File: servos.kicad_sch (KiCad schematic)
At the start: 28 parts, among them J10 Conn_01x03_Male, J5 Conn_01x03_Male, J6 Conn_01x03_Male, J7 Conn_01x03_Male, J8 Conn_01x03_Male, J9 Conn_01x03_Male, U2 MOCD20, U3 MOCD20, U4 MOCD20, U5 MOCD20

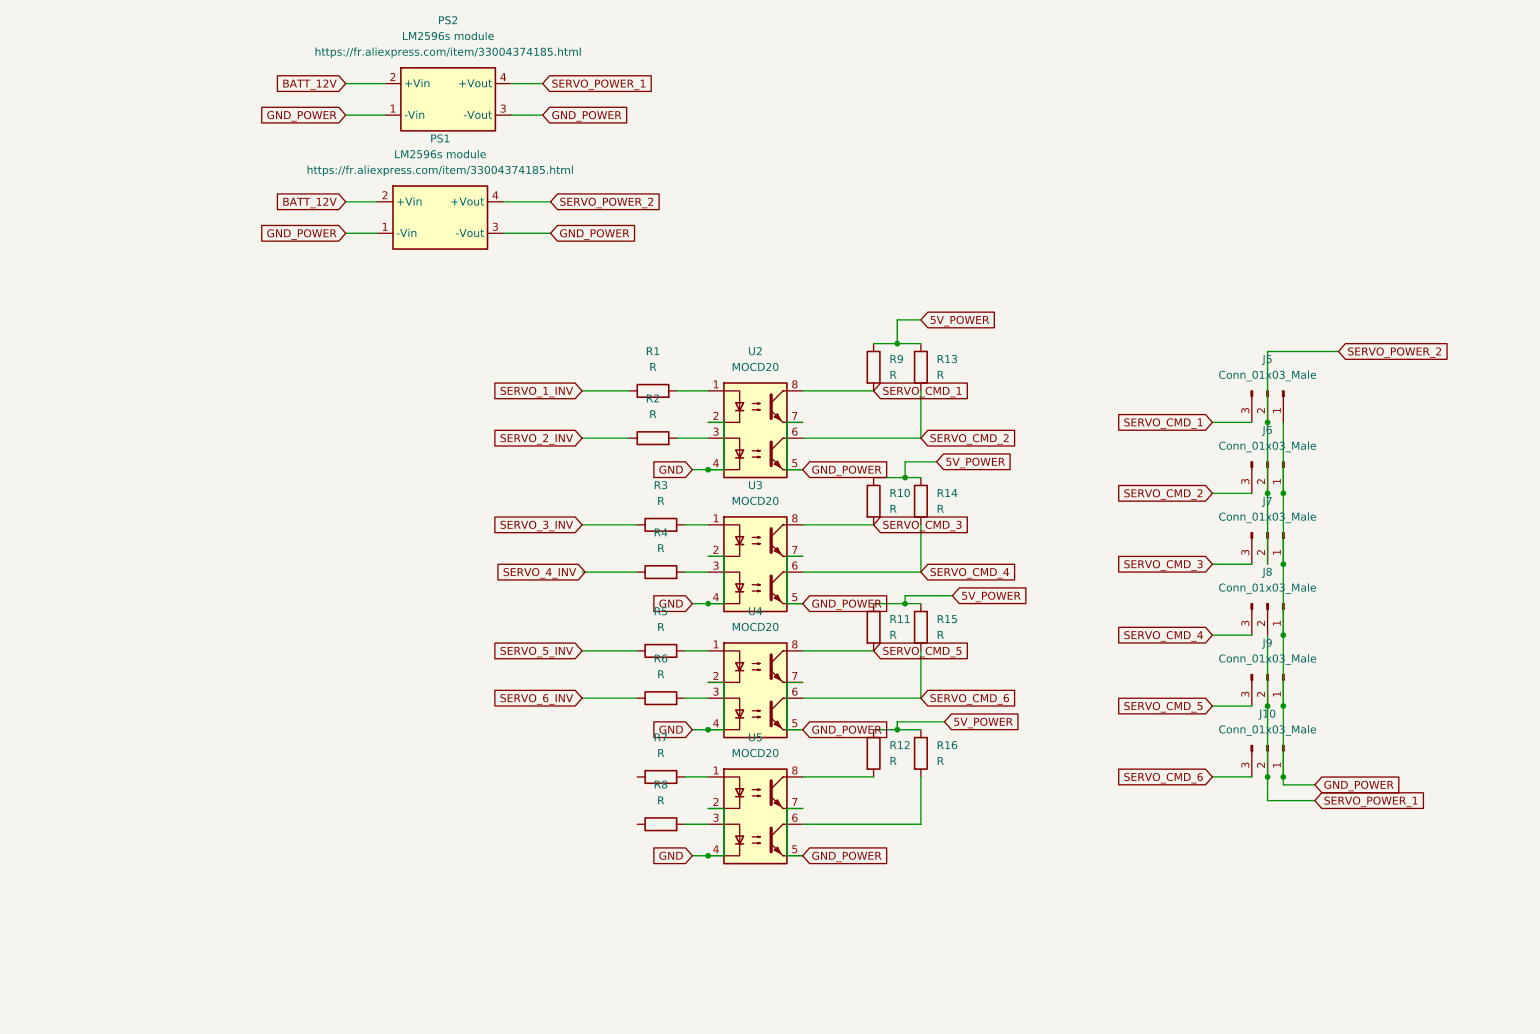
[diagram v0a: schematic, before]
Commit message: version without mega I2C pins
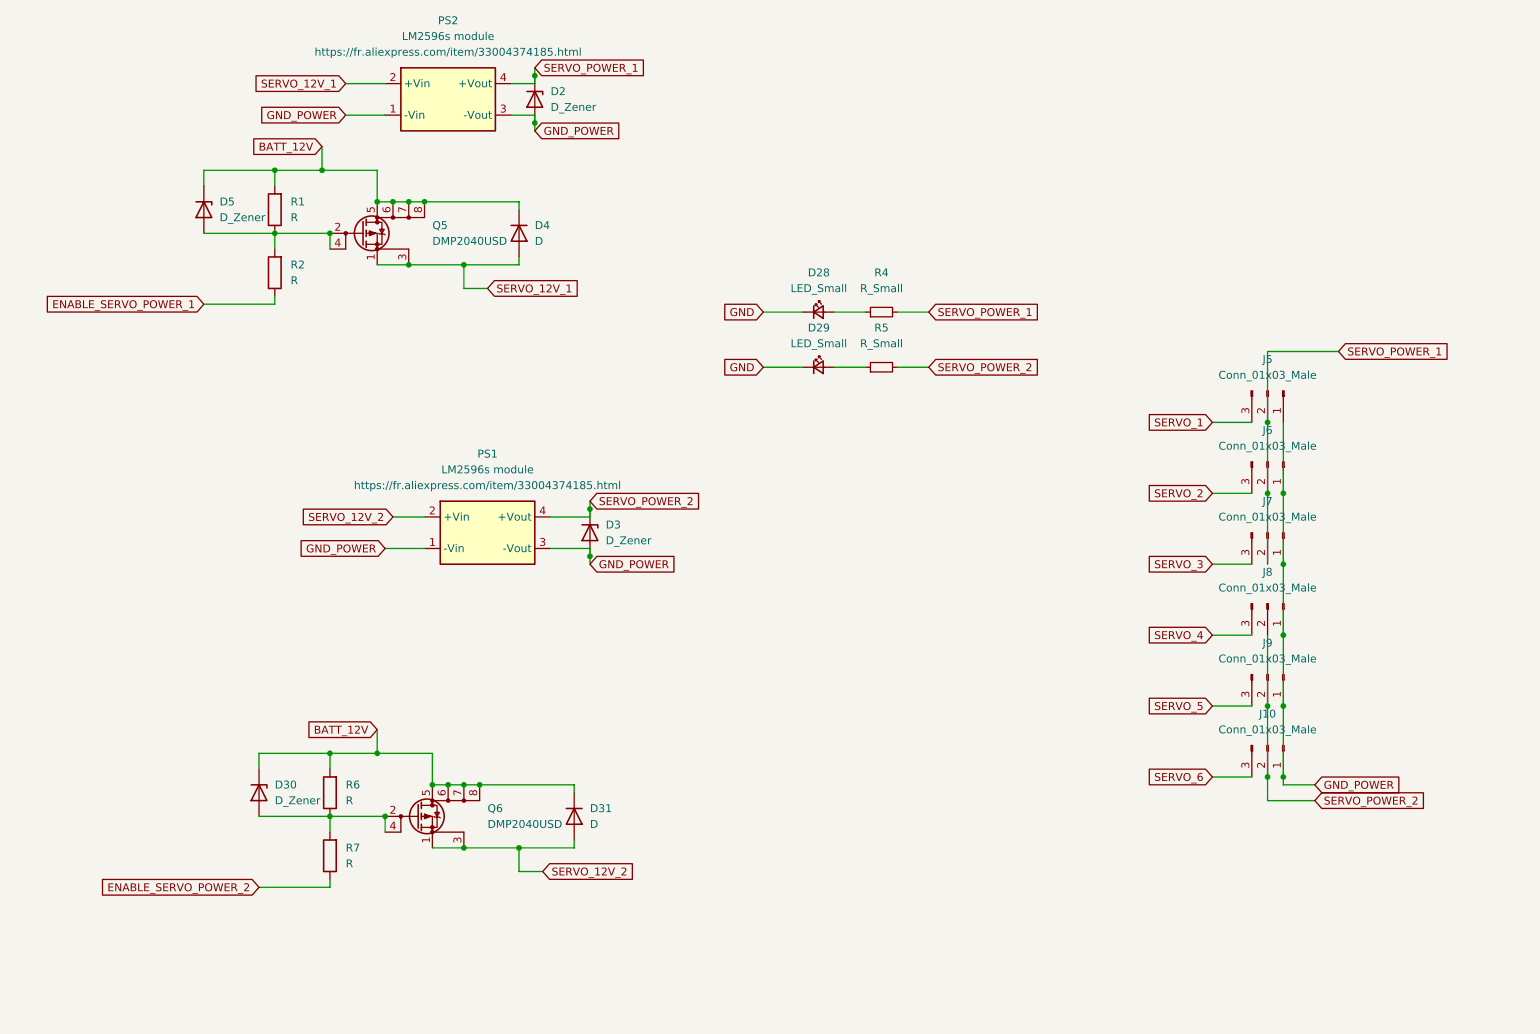
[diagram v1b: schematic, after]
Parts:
- removed R10, R11, R12, R13, R14, R15, R16, R3, R4, R5, R8, R9: R, Resistor_SMD:R_0603_1608Metric, symbol Device:R
- removed U2, U3, U4, U5: MOCD20, Package_SO:SO-8_3.9x4.9mm_P1.27mm, symbol New_Library_Victor:MOCD20
- added D2, D3, D30, D5: D_Zener, Diode_SMD:D_1206_3216Metric, symbol Device:D_Zener
- added D28, D29: LED_Small, LED_SMD:LED_0805_2012Metric, symbol Device:LED_Small
- added D31, D4: D, Diode_SMD:D_1206_3216Metric, symbol Device:D
- added Q5, Q6: DMP2040USD, Package_SO:SO-8_3.9x4.9mm_P1.27mm, symbol New_Library_Victor:DMP2040USD
- added R4, R5: R_Small, Resistor_SMD:R_0603_1608Metric, symbol Device:R_Small
- PS1, PS2: footprint LibraryVictor:lm2596Module -> Converter_DCDC:Converter_DCDC
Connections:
- net SERVO_1_INV is gone; now on an unnamed net: R1.1
- net SERVO_6_INV is gone; now on an unnamed net: R6.1
- net BATT_12V: now also R1.2, R6.2, D30.1 (K), D31.1 (K), D4.1 (K), D5.1 (K), Q5.5 (D), Q5.6 (D), Q5.7 (D), Q5.8 (D), Q6.5 (D), Q6.6 (D), Q6.7 (D), Q6.8 (D); no longer PS1.2 (+Vin), PS2.2 (+Vin)
- net GND: now also D28.1 (K), D29.1 (K)
- net GND_POWER: now also D2.2 (A), D3.2 (A)
- net SERVO_POWER_1: now also J5.2 (Pin_2), J6.2 (Pin_2), J7.2 (Pin_2), D2.1 (K), R4.2; no longer J10.2 (Pin_2), J8.2 (Pin_2), J9.2 (Pin_2)
- net SERVO_POWER_2: now also J10.2 (Pin_2), J8.2 (Pin_2), J9.2 (Pin_2), D3.1 (K), R5.2; no longer J5.2 (Pin_2), J6.2 (Pin_2), J7.2 (Pin_2)
- net ENABLE_SERVO_POWER_2: now reaches R7.1
- net at R7.2: now also D30.2 (A), Q6.2 (G), Q6.4 (G)
- net at R2.2: now also D5.2 (A), Q5.2 (G), Q5.4 (G)
- net SERVO_2_INV renamed ENABLE_SERVO_POWER_1
- net SERVO_CMD_1 renamed SERVO_1
- net SERVO_CMD_2 renamed SERVO_2
- net SERVO_CMD_3 renamed SERVO_3
- net SERVO_CMD_4 renamed SERVO_4
- net SERVO_CMD_5 renamed SERVO_5
- net SERVO_CMD_6 renamed SERVO_6
- new net: D28.2 (A), R4.1
- new net: D29.2 (A), R5.1
- new net SERVO_12V_1: D4.2 (A), PS2.2 (+Vin), Q5.1 (S), Q5.3 (S)
- new net SERVO_12V_2: D31.2 (A), PS1.2 (+Vin), Q6.1 (S), Q6.3 (S)
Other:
- moved on the sheet: PS1

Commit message: small fixes
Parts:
- added J18, J19: Conn_01x03_Male, Connector_PinSocket_2.54mm:PinSocket_1x03_P2.54mm_Vertical, symbol Connector:Conn_01x03_Male
- PS1, PS2: footprint Converter_DCDC:Converter_DCDC -> LibraryVictor:lm2596Module
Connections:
- net GND_POWER: now also J18.1 (Pin_1), J19.1 (Pin_1)
- net SERVO_POWER_1: now also J18.2 (Pin_2)
- net SERVO_POWER_2: now also J19.2 (Pin_2)
- new net SERVO_7: J18.3 (Pin_3)
- new net SERVO_8: J19.3 (Pin_3)
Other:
- moved on the sheet: J5, J6, J7

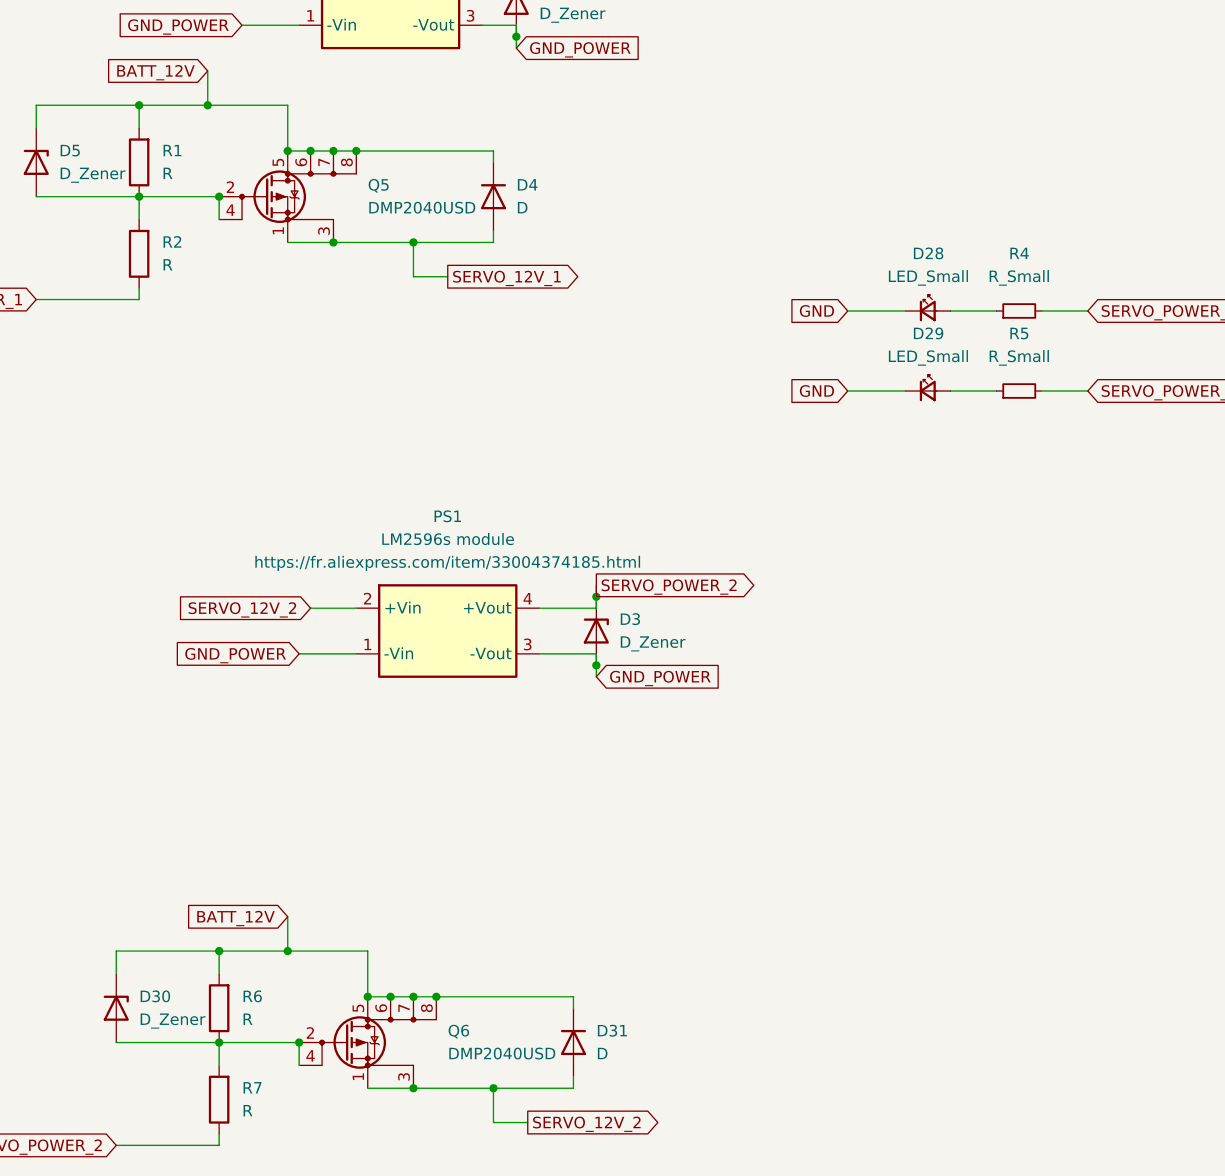
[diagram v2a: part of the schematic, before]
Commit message: specify values + BOM
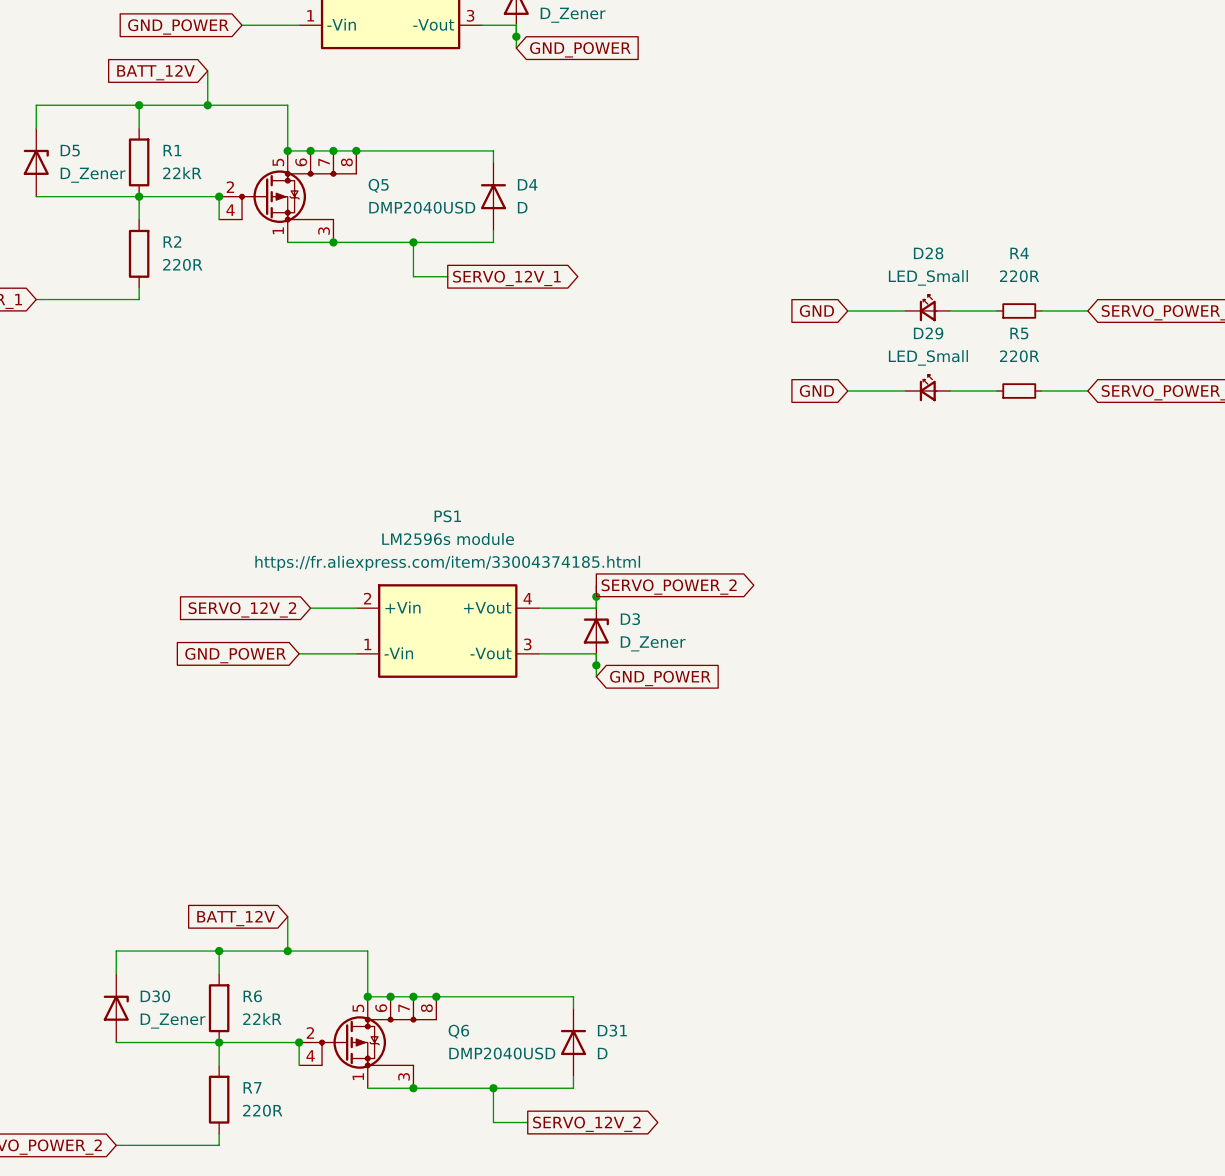
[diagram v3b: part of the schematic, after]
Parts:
- R1, R6: value R -> 22kR
- R2, R7: value R -> 220R
- R4, R5: value R_Small -> 220R
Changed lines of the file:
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@@
       (effects (font (size 1.27 1.27)) (justify right))
     )
-    (property "Value" "R" (id 1) (at 62.23 151.1299 0)
+    (property "Value" "22kR" (id 1) (at 62.23 151.1299 0)
       (effects (font (size 1.27 1.27)) (justify right))
     )
@@
     (in_bom yes) (on_board yes) (fields_autoplaced)
     (property "Reference" "R5" (id 0) (at 148.59 74.93 90))
-    (property "Value" "R_Small" (id 1) (at 148.59 77.47 90))
+    (property "Value" "220R" (id 1) (at 148.59 77.47 90))
     (property "Footprint" "Resistor_SMD:R_0603_1608Metric" (id 2) (at 148.59 81.28 0)
       (effects (font (size 1.27 1.27)) hide)
@@
       (effects (font (size 1.27 1.27)) (justify right))
     )
-    (property "Value" "R" (id 1) (at 62.23 161.2899 0)
+    (property "Value" "220R" (id 1) (at 62.23 161.2899 0)
       (effects (font (size 1.27 1.27)) (justify right))
     )
@@
     (in_bom yes) (on_board yes) (fields_autoplaced)
     (property "Reference" "R4" (id 0) (at 148.59 66.04 90))
-    (property "Value" "R_Small" (id 1) (at 148.59 68.58 90))
+    (property "Value" "220R" (id 1) (at 148.59 68.58 90))
     (property "Footprint" "Resistor_SMD:R_0603_1608Metric" (id 2) (at 148.59 72.39 0)
       (effects (font (size 1.27 1.27)) hide)
@@
       (effects (font (size 1.27 1.27)) (justify right))
     )
-    (property "Value" "R" (id 1) (at 53.34 57.1499 0)
+    (property "Value" "22kR" (id 1) (at 53.34 57.1499 0)
       (effects (font (size 1.27 1.27)) (justify right))
     )
@@
       (effects (font (size 1.27 1.27)) (justify right))
     )
-    (property "Value" "R" (id 1) (at 53.34 67.3099 0)
-      (effects (font (size 1.27 1.27)) (justify right))
-    )
+    (property "Value" "220R" (id 1) (at 53.34 67.3099 0)
+      (effects (font (size 1.27 1.27)) (justify right))
+    )

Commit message: [WiP] debut de V2
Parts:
- added C5, C6: C_Polarized_Small, Capacitor_THT:CP_Radial_D8.0mm_P2.50mm, symbol Device:C_Polarized_Small
- added D34, D35: D, Diode_SMD:D_1206_3216Metric, symbol Device:D
- added Q8, Q9: Q_NMOS_DGS, symbol Device:Q_NMOS_DGS
- added R13: 220R, Resistor_SMD:R_0603_1608Metric, symbol Device:R
- added R14: 2.2kR, Resistor_SMD:R_0603_1608Metric, symbol Device:R
- R7: value 220R -> 2.2kR
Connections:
- net ENABLE_SERVO_POWER_2: now also R13.1; no longer R7.1
- net GND: now also Q8.3 (S), Q9.3 (S)
- net GND_POWER: now also C5.2, C6.2, D34.2 (A), D35.2 (A)
- net SERVO_POWER_1: now also C6.1, D35.1 (K)
- net SERVO_POWER_2: now also C5.1, D34.1 (K)
- net at D5.2 (A), Q5.2 (G), Q5.4 (G)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: now also R14.1; no longer R2.2
- new net: Q9.1 (D), R7.1
- new net: Q9.2 (G), R13.2
- new net: Q8.1 (D), R14.2
- new net: Q8.2 (G), R2.2
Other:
- moved on the sheet: R2
